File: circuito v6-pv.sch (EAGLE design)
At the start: 67 parts, among them IC1 LM324N

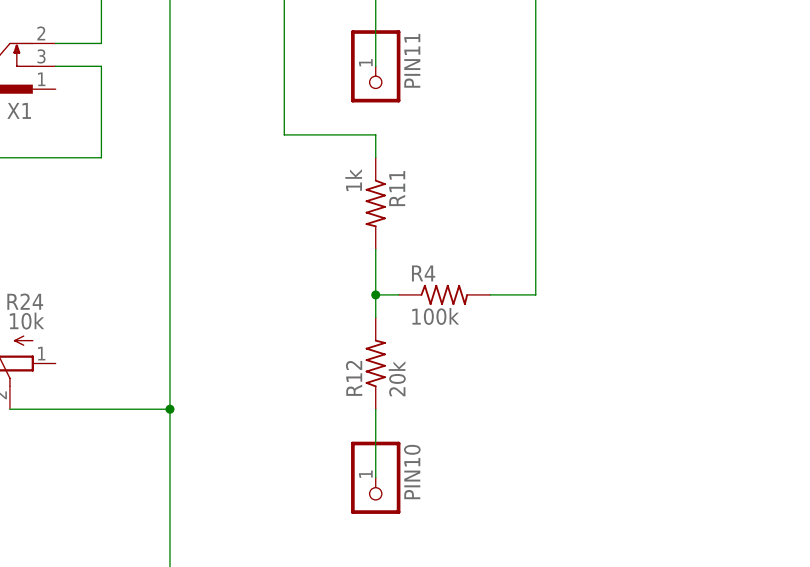
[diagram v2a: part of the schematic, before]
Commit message: Actualizacion de resistencias para ruido
Resistencias 200k, 100k y 10k dejan un volumen de ruido tal que no es muy molesto con el estimulo
pero lo suficientemente molesto porque es lo que da el valor maximo
el chiste seria manejar el ruido desde el soft despues
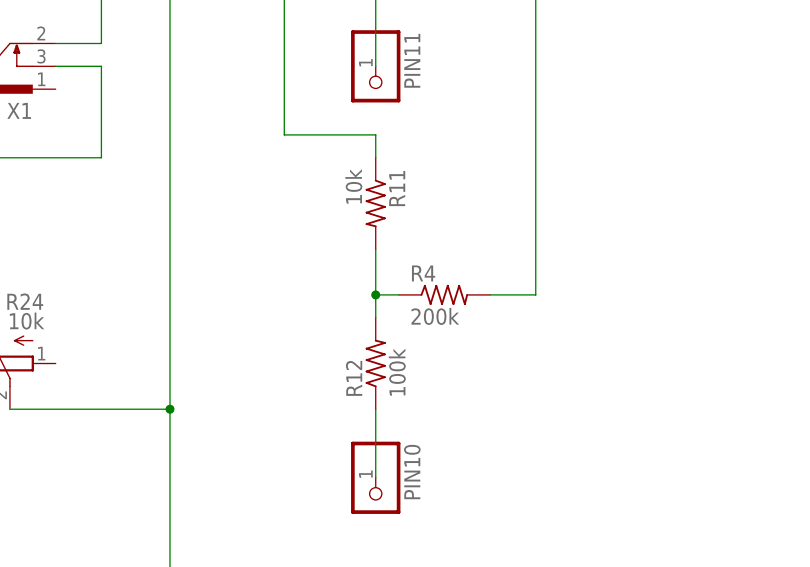
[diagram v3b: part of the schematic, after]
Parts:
- R11: value 1k -> 10k
- R12: value 20k -> 100k
- R4: value 100k -> 200k
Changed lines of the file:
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@@
 <attribute name="SPICEPREFIX" value="X"/>
 </part>
-<part name="R11" library="rcl" library_urn="urn:adsk.eagle:library:334" deviceset="R-US_" device="0207/7" package3d_urn="urn:adsk.eagle:package:23493/1" value="1k">
-<spice>
-<pinmapping isusermap="yes" isdevicewide="yes">
-<pinmap gate="G$1" pin="1" pinorder="1"/>
-<pinmap gate="G$1" pin="2" pinorder="2"/>
-</pinmapping>
-</spice>
-</part>
-<part name="R12" library="rcl" library_urn="urn:adsk.eagle:library:334" deviceset="R-US_" device="0207/7" package3d_urn="urn:adsk.eagle:package:23493/1" value="20k">
+<part name="R11" library="rcl" library_urn="urn:adsk.eagle:library:334" deviceset="R-US_" device="0207/7" package3d_urn="urn:adsk.eagle:package:23493/1" value="10k">
+<spice>
+<pinmapping isusermap="yes" isdevicewide="yes">
+<pinmap gate="G$1" pin="1" pinorder="1"/>
+<pinmap gate="G$1" pin="2" pinorder="2"/>
+</pinmapping>
+</spice>
+</part>
+<part name="R12" library="rcl" library_urn="urn:adsk.eagle:library:334" deviceset="R-US_" device="0207/7" package3d_urn="urn:adsk.eagle:package:23493/1" value="100k">
 <spice>
 <pinmapping isusermap="yes" isdevicewide="yes">
@@
 </part>
 <part name="S1" library="switch" library_urn="urn:adsk.eagle:library:380" deviceset="320-938" device="" package3d_urn="urn:adsk.eagle:package:27685/1"/>
-<part name="R4" library="rcl" library_urn="urn:adsk.eagle:library:334" deviceset="R-US_" device="0207/7" package3d_urn="urn:adsk.eagle:package:23493/1" value="100k">
-<spice>
-<pinmapping isusermap="yes" isdevicewide="yes">
+<part name="R4" library="rcl" library_urn="urn:adsk.eagle:library:334" deviceset="R-US_" device="0207/7" package3d_urn="urn:adsk.eagle:package:23493/1" value="200k">
+<spice>
+<pinmapping isusermap="yes" isdevicewide="yes">

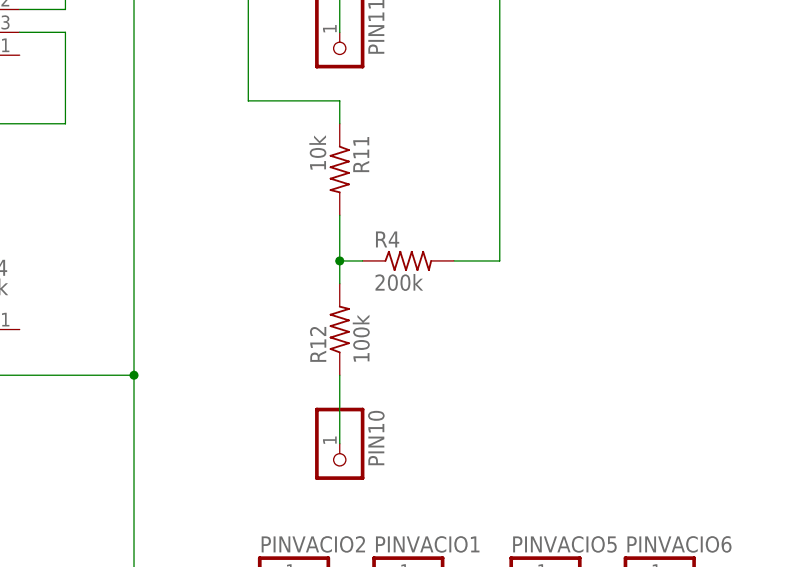
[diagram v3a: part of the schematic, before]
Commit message: Actualizacion R fija para ruido 32k
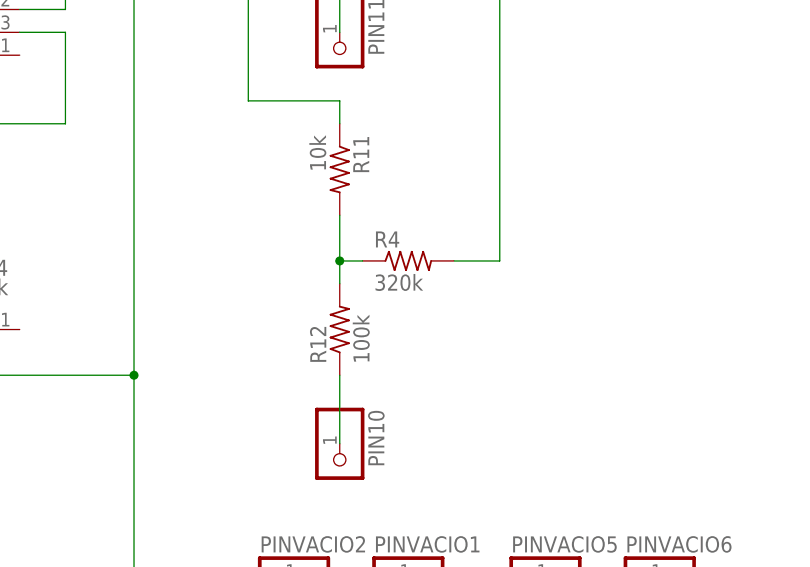
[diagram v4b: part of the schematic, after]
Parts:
- R4: value 200k -> 320k
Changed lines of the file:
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@@
 </part>
 <part name="S1" library="switch" library_urn="urn:adsk.eagle:library:380" deviceset="320-938" device="" package3d_urn="urn:adsk.eagle:package:27685/1"/>
-<part name="R4" library="rcl" library_urn="urn:adsk.eagle:library:334" deviceset="R-US_" device="0207/7" package3d_urn="urn:adsk.eagle:package:23493/1" value="200k">
+<part name="R4" library="rcl" library_urn="urn:adsk.eagle:library:334" deviceset="R-US_" device="0207/7" package3d_urn="urn:adsk.eagle:package:23493/1" value="320k">
 <spice>
 <pinmapping isusermap="yes" isdevicewide="yes">
